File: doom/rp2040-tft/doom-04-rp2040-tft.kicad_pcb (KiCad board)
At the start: 4 copper layers, 132 x 104 mm, 92 parts, among them J4 DM3AT-SF-PEJM5, J5 S2B-PH-K-S(LF)(SN), Q1 AO3401A, Q2 FS8205A, SW1 PTS645SM43SMTR92 LFS, SW2 PTS645SM43SMTR92 LFS, SW3 PTS645SM43SMTR92 LFS, SW4 PTS645SM43SMTR92 LFS, SW5 PTS645SM43SMTR92 LFS, SW6 PTS645SM43SMTR92 LFS, SW7 PTS645SM43SMTR92 LFS, SW8 PTS645SM43SMTR92 LFS, SW9 MSK12C02, U1 RP2040, U2 DW01A, U3 W25Q128JVSIQ, U4 TLV75533PDBVR, U5 PAM8403DR, U6 BQ24075RGTR, U7 ESD 2-line, Y1 12MHz 10pF

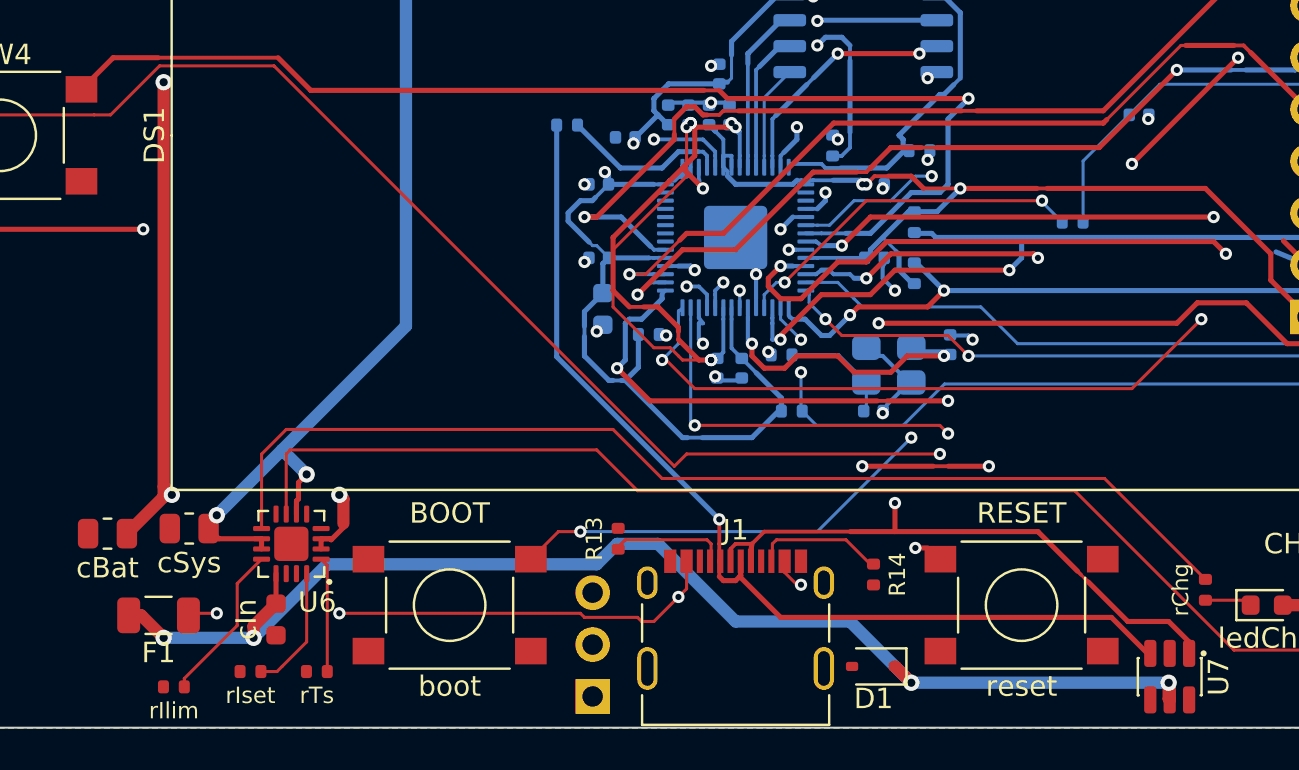
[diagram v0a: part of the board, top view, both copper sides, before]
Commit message: doom, examples: re-route around the USB-C receptacle's new land pattern
The standard receptacle became GCT USB4105's recommended layout (pcbkit 7e43c086): its shield
legs moved and two unplated guide holes appeared, under the copper these boards had been routed
with (solder-mask-bridge and clearance errors at J1). `build.run` re-routed the 3–5 nets that
crossed it: all seven check complete with 0 errors again; the six Doom boards export for the fab
without --force.

Claude-Session: https://claude.ai/code/session_01GffCzZXi9ShujPbky1eccg
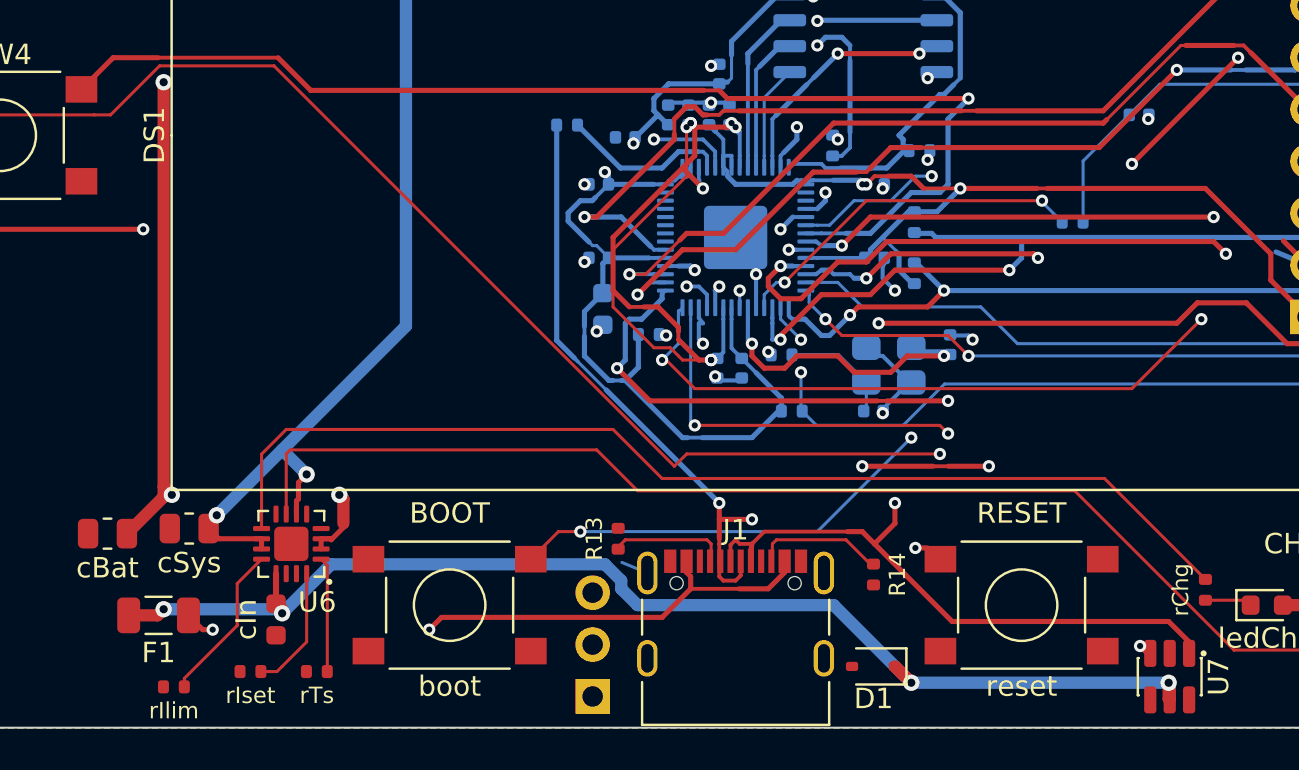
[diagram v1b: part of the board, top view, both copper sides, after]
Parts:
- F1: value PTC 1000mA -> PTC 750mA
- J1: value (none) -> USB4105-GF-A
- U7: value ESD 2-line -> USBLC6-2SC6
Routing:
- net VBUS: track 62.5 -> 60.3 mm
- net CONN_DN: track 49.1 -> 51.2 mm, vias 1 -> 3
- net usb/power/raw: track 34.5 -> 32.6 mm, vias 4 -> 2
- net GND: track 13.8 -> 15.2 mm
- net CONN_DP: track 48.3 -> 49.6 mm
- net SWCLK: track 25.0 -> 24.1 mm

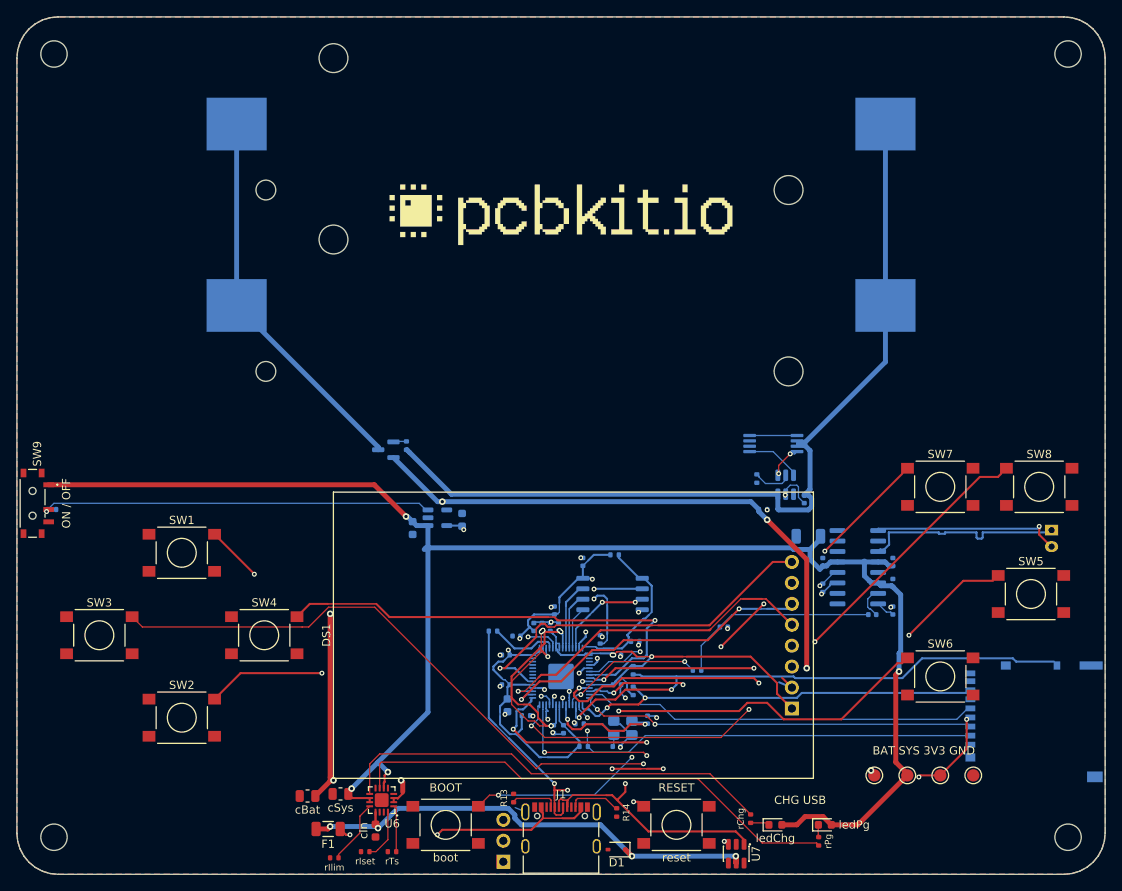
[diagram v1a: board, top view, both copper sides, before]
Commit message: Boards pass check and KiCad 10's DRC again: holes in courtyards, the USB net rename
pcbkit's check now has KiCad 10's pth/npth_inside_courtyard (pcbkit be5b6955), and 13 boards
failed it. KiCad's own DRC (kicad-cli 10) reports the same holes on every one of them.

- Parts that really stand above the holes under them (a screen or a Nano on its sockets, the
  Delta-S02's КМ-6 capacitors flat under its chips, as the factory placed them): a courtyard rule
  for the pair, written to each board's .kicad_dru, so KiCad's DRC agrees.
- Real collisions moved: servo-controller's dial 3 mm up (the Nano's socket pins came out under
  it), c3-pocket's fourth M3 hole from under a cell holder to the top edge's middle, s3-rgb's
  D-pad 2 mm up (a holder's peg came through under the down key).
- v003-emu, c3-pocket, rp2040-tft, rp2350-psram, s3-rgb, teensy41: re-routed for the standard USB
  block's renamed net (usb/raw is usb/vbusIn since pcbkit 2088839e): their tracks still carried
  the old name and shorted the fuse and connector pads.
- p4-touch-7: its board file still had a courtyard for the panel the design gives none (KiCad
  reported 114 courtyard errors); written again.

Measured on the dev host: all 44 registry boards `pcbkit check` complete with 0 errors, and
kicad-cli pcb drc 0 errors on every board.

Claude-Session: https://claude.ai/code/session_018URVYF1YPgyrMNetY9yT1T
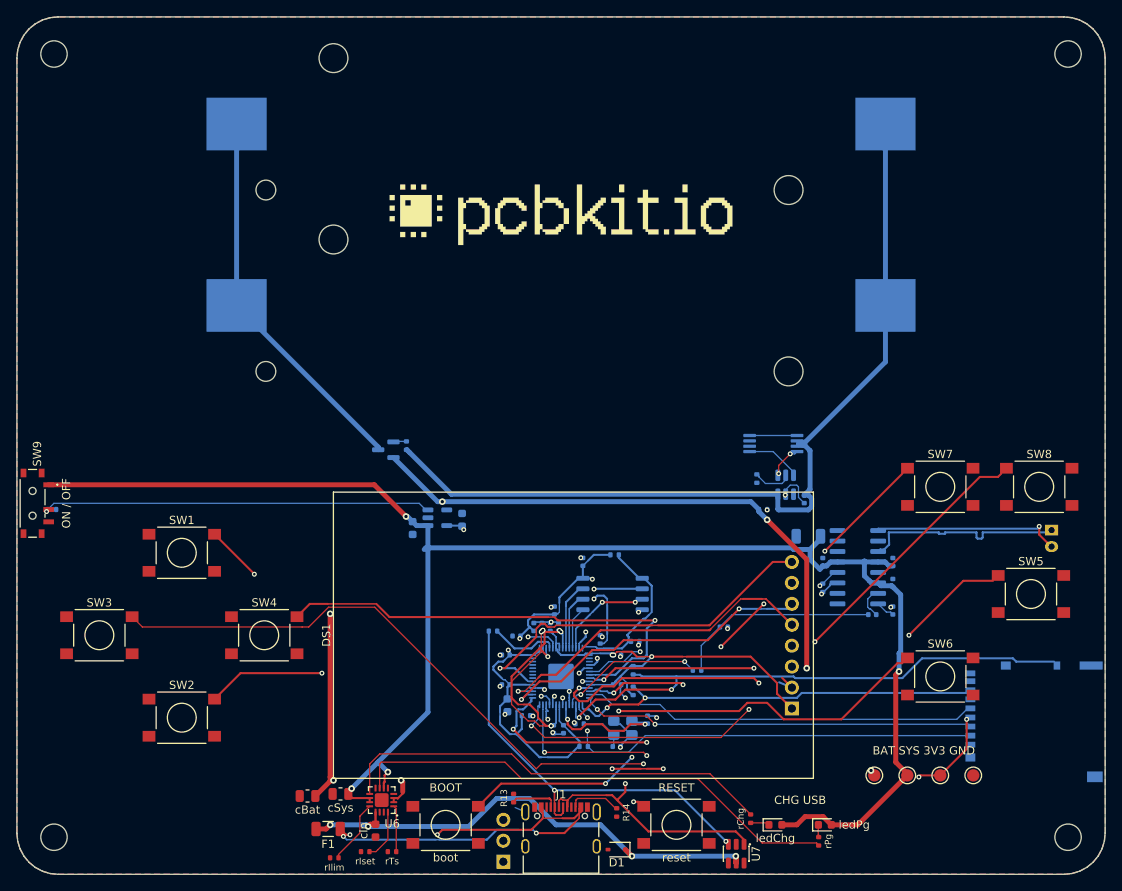
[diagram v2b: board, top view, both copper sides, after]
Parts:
- H1, H2, H3, H4: value (none) -> MountingHole_3.2mm_M3
- J3: value (none) -> PinHeader_1x03_P2.54mm_Vertical
- logo: value (none) -> Logo_PCBKit_pcbkit.io
- tpBat, tpGnd, tpSys, tpV3: value (none) -> TestPoint_Round_D1.5mm
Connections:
- net usb/power/raw renamed usb/power/vbusIn
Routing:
- net usb/power/vbusIn: track 32.6 -> 66.3 mm, vias 2 -> 4
- net DVDD: track 49.1 -> 50.0 mm
- net VBUS: track 60.3 -> 60.8 mm
- net CONN_DN: track 51.2 -> 50.7 mm, vias 3 -> 2

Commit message: doom: a resettable fuse per 18650 cell, a 2 % backlight clamp, a 1 A LDO on the S3 boards
The verifier (wiring-parallel-cells) found the two holders of every Doom board directly in parallel:
a cell put in backwards, or one much fuller than the other, drives the other through nothing but
the cells' resistance (about 56-168 A). Each holder's + now reaches BAT_IN through its own 2 A
resettable fuse (Littelfuse 1812L200/16GR, C18198340: 16 V, 100 A interrupting) on new nets
CELL1_P / CELL2_P. Nothing else moved; the boards were re-routed for the new nets.

- s3-rgb: the MT3608 backlight's open-panel clamp was a 28 V 5 % zener (bound 30.0 V against the
  switch's 30 V). It is now two 2 % zeners in series, UDZVTE-1718B + UDZVTE-1710B (27.33-28.56 V;
  LCSC stocks no single 28 V 2 % part). That is under 29.2 V and above the panel's 27.2 V.
- s3-rgb, s3-handheld: TLV75533 (500 mA) -> TLV75733 (1 A, C485517, same DBV pins; sheet from
  SBVS322C), for the ESP32-S3's 500 mA supply peaks (erc-supply-peak).
- c3-pocket, v003-emu: the USB PTC's hold is 750 mA, as the part (nSMD075) is (rating-current).
- pico2-carrier: the CHG/PG LEDs 1.5 mm further from the display's courtyard. rp2350-handheld:
  the logo off the LCD's courtyard and BT1's peg.
- READMEs: the per-cell fuses, the boards already ordered (s3-rgb, JLC W2026102705013253: insert
  the cells one at a time), status and BOM as check and the fab export give them now.

Measured on the dev host (pcbkit 5e0d2cc8): all 11 complete, 0 errors, 0 unrouted. What is left is
erc-rail-name (sent to the verifier as false positives) and full-speed USB pair coupling. The MCU
pins' nets are unchanged on every board, so the firmware and its simulation are unchanged.

Claude-Session: https://claude.ai/code/session_01B3VRfBCg9vAvGVWujVGarr
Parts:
- added F2: PTC 2000mA, Fuse_1812_4532Metric, B.Cu at (120.8, 135.8)
- added F3: PTC 2000mA, Fuse_1812_4532Metric, B.Cu at (120.8, 113.8)
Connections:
- BT1 pad 2: BAT_IN -> CELL1_P
- BT2 pad 2: BAT_IN -> CELL2_P
- SW1 pad 2: UP -> GND
- SW2 pad 2: DOWN -> GND
- SW3 pad 2: LEFT -> GND
- SW4 pad 2: RIGHT -> GND
- SW5 pad 2: FIRE -> GND
- SW6 pad 2: USE -> GND
- SW7 pad 2: SELECT -> GND
- SW8 pad 2: START -> GND
- boot pad 2: BOOTSEL -> GND
- reset pad 2: RUN -> GND
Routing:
- net CELL1_P: track 0.00 -> 6.98 mm
- net CELL2_P: track 0.00 -> 6.98 mm
- net BAT_IN: track 46.6 -> 52.0 mm

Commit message: boards: 15 boards rebuilt on pcbkit 20ffacdc9 (their pours under the 0.25 mm hole clearance)
Every board checked with main: 17 of 44 failed on hole-clearance (pours filled before fill c6 made
0.25 mm KiCad's hole clearance the default), keepout (holes now sized by the board) or
place-corner. design.run {} on each (placement and routing kept, pours refilled): 15 now complete,
0 errors. Not here: esp32-p4-touch-lcd-7b and p4-touch-7 (a build reroutes their pairs: 21 and 7
unrouted; kept as they were, 2,372 and 919 hole-clearance errors: a refill without a reroute is
needed).

Claude-Session: https://claude.ai/code/session_01BAgp959tApA8aEg85EYgfb
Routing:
- net usb/power/vbusIn: track 66.3 -> 71.5 mm, vias 4 -> 6
- net VBUS: track 60.8 -> 60.3 mm
